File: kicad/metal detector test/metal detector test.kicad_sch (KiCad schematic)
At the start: 108 parts, among them J1 3.5mm audio jack TRS, Q1 PNP, Q2 NPN, SW0 SW_SPST, SW1 SW_SPST, SW10 SW_SPST, SW2 SW_SPST, SW3 SW_SPST, SW4 SW_SPST, SW5 SW_SPST, SW6 SW_SPST, SW7 SW_SPST, SW8 SW_SPST, U1 op amp (higher voltage), U10 3.3v lin reg, U11 lp filter, U12 op amp (lower voltage), U2 nucleo-32 uC module, U3 9v lin reg, U4 5v lin reg, U5 3.3v lin reg, U6 audio amp, U7 lp filter, U8 switch debounce, U9 5v lin reg

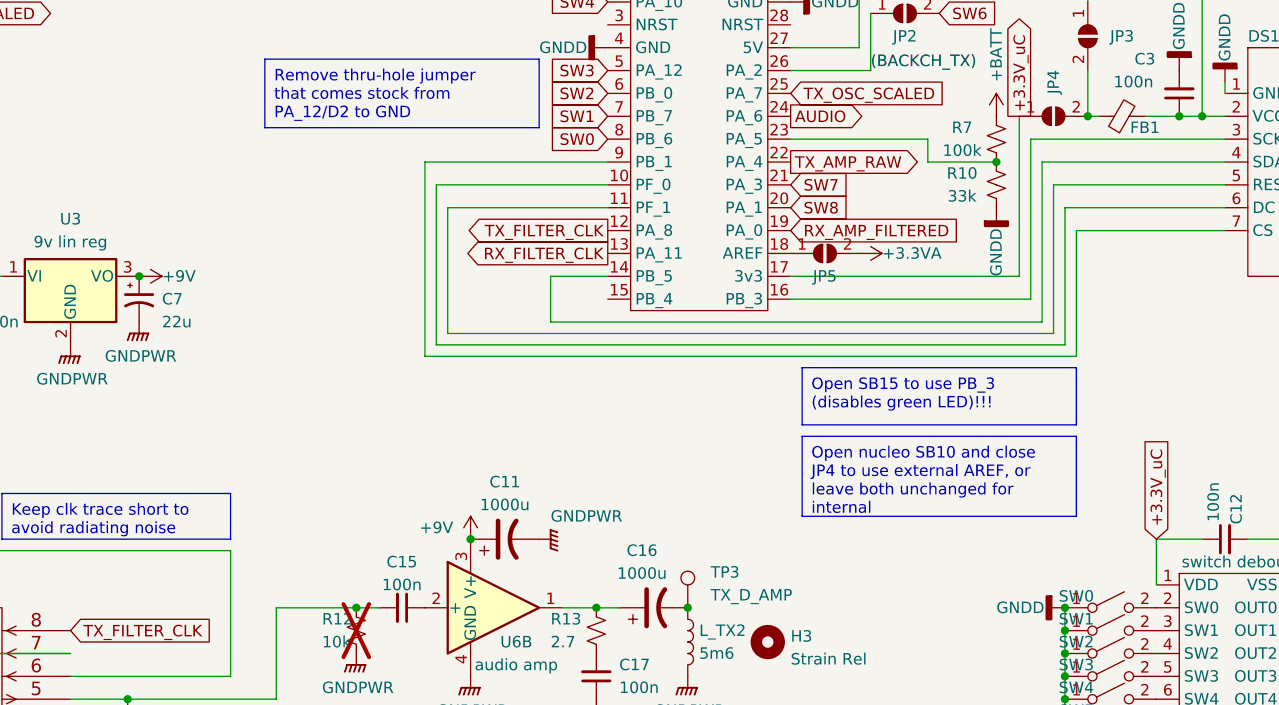
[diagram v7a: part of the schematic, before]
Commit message: Realized that I was accidentially using a pin required to use the external 8 MHz MCO xtal signal passed from the debugger chip, changed to another one.
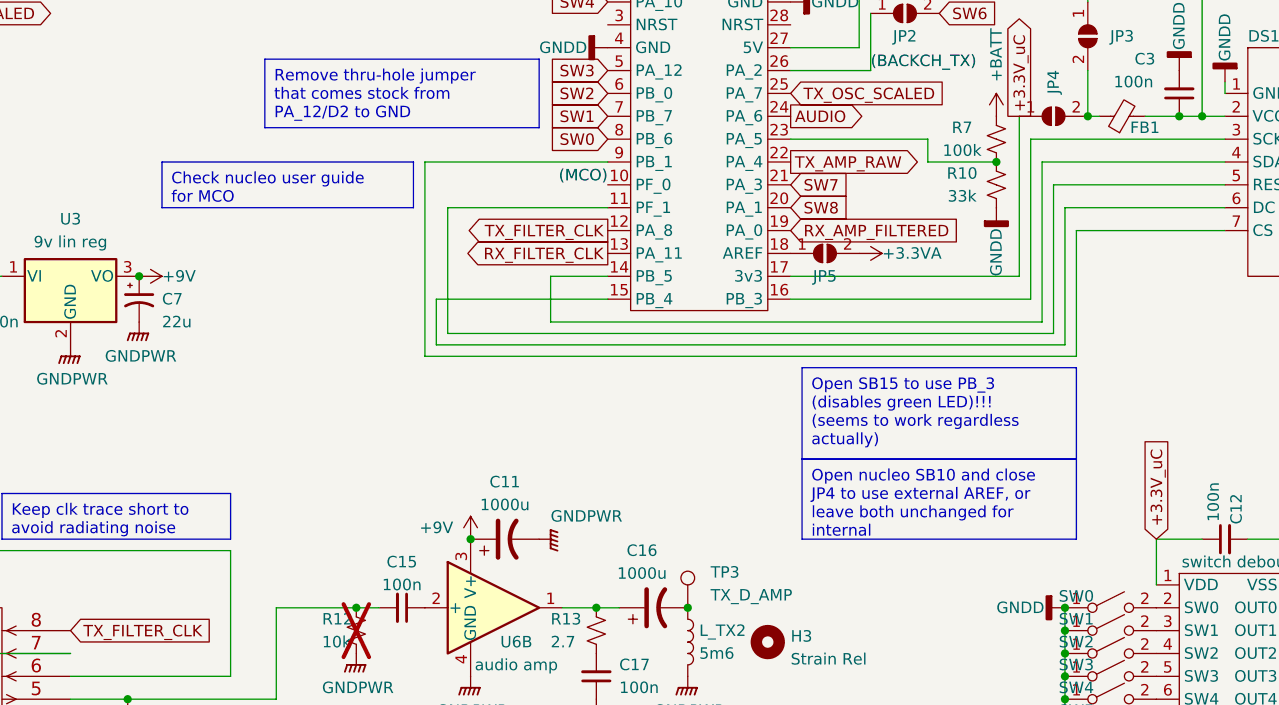
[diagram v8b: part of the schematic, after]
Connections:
- net at DS1.6 (DC): now also U2.15 (PB_4); no longer U2.10 (PF_0)
- new net (MCO): U2.10 (PF_0)
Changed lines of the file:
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@@
+    (stroke (width 0) (type default))
+  )
+  (wire (pts (xy 177.8 63.5) (xy 177.8 68.58))
     (stroke (width 0) (type default))
   )
@@
     (stroke (width 0) (type default))
   )
+  (wire (pts (xy 196.85 63.5) (xy 177.8 63.5))
+    (stroke (width 0) (type default))
+  )
   (wire (pts (xy 27.94 190.5) (xy 27.94 180.34))
     (stroke (width 0) (type default))
@@
     (stroke (width 0) (type default))
   )
-  (wire (pts (xy 196.85 50.8) (xy 177.8 50.8))
-    (stroke (width 0) (type default))
-  )
   (wire (pts (xy 115.57 24.13) (xy 115.57 26.67))
     (stroke (width 0) (type default))
@@
     (stroke (width 0) (type default))
   )
-  (wire (pts (xy 177.8 50.8) (xy 177.8 68.58))
-    (stroke (width 0) (type default))
-  )
   (wire (pts (xy 73.66 20.32) (xy 72.39 20.32))
     (stroke (width 0) (type default))
@@
   )
   (text_box "Open nucleo SB10 and close JP4 to use external AREF, or leave both unchanged for internal"
-    (at 218.44 78.74 0) (size 30.48 8.89)
+    (at 218.44 81.28 0) (size 30.48 8.89)
     (stroke (width 0) (type default))
     (fill (type none))
@@
     (effects (font (size 1.27 1.27)) (justify left top))
   )
-  (text_box "Open SB15 to use PB_3 (disables green LED)!!!"
-    (at 218.44 71.12 0) (size 30.48 6.35)
+  (text_box "Open SB15 to use PB_3 (disables green LED)!!! (seems to work regardless actually)"
+    (at 218.44 71.12 0) (size 30.48 10.16)
     (stroke (width 0) (type default))
     (fill (type none))
@@
     (effects (font (size 1.27 1.27)) (justify left top))
   )
+  (text_box "Check nucleo user guide for MCO"
+    (at 147.32 48.26 0) (size 27.94 5.08)
+    (stroke (width 0) (type default))
+    (fill (type none))
+    (effects (font (size 1.27 1.27)) (justify left top))
+  )
   (text "(µC)" (at 52.07 92.71 0)
     (effects (font (size 1.27 1.27)) (justify left bottom))
@@
     (effects (font (size 1.27 1.27)) (justify left bottom))
   )
+  (label "(MCO)" (at 196.85 50.8 180) (fields_autoplaced)
+    (effects (font (size 1.27 1.27)) (justify right bottom))
+  )
   (label "(BACKCH_TX)" (at 226.06 38.1 0) (fields_autoplaced)
